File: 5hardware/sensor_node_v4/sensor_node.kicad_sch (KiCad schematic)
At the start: 19 parts, among them J4 Conn_02x20_Counter_Clockwise, J5 Conn_02x20_Counter_Clockwise, SW7 SW_DIP_x04, SW8 SW_Push, SW9 RotaryEncoder, U10 CH32V003F4P6, U11 MCP1700x-330xxTO, U12 APDS-9960, U14 DS3231M, U15 DS1307+, U16 DS1302+, U17 VL53L1CXV0FY1, U18 BH1750FVI-TR, Y1 Crystal

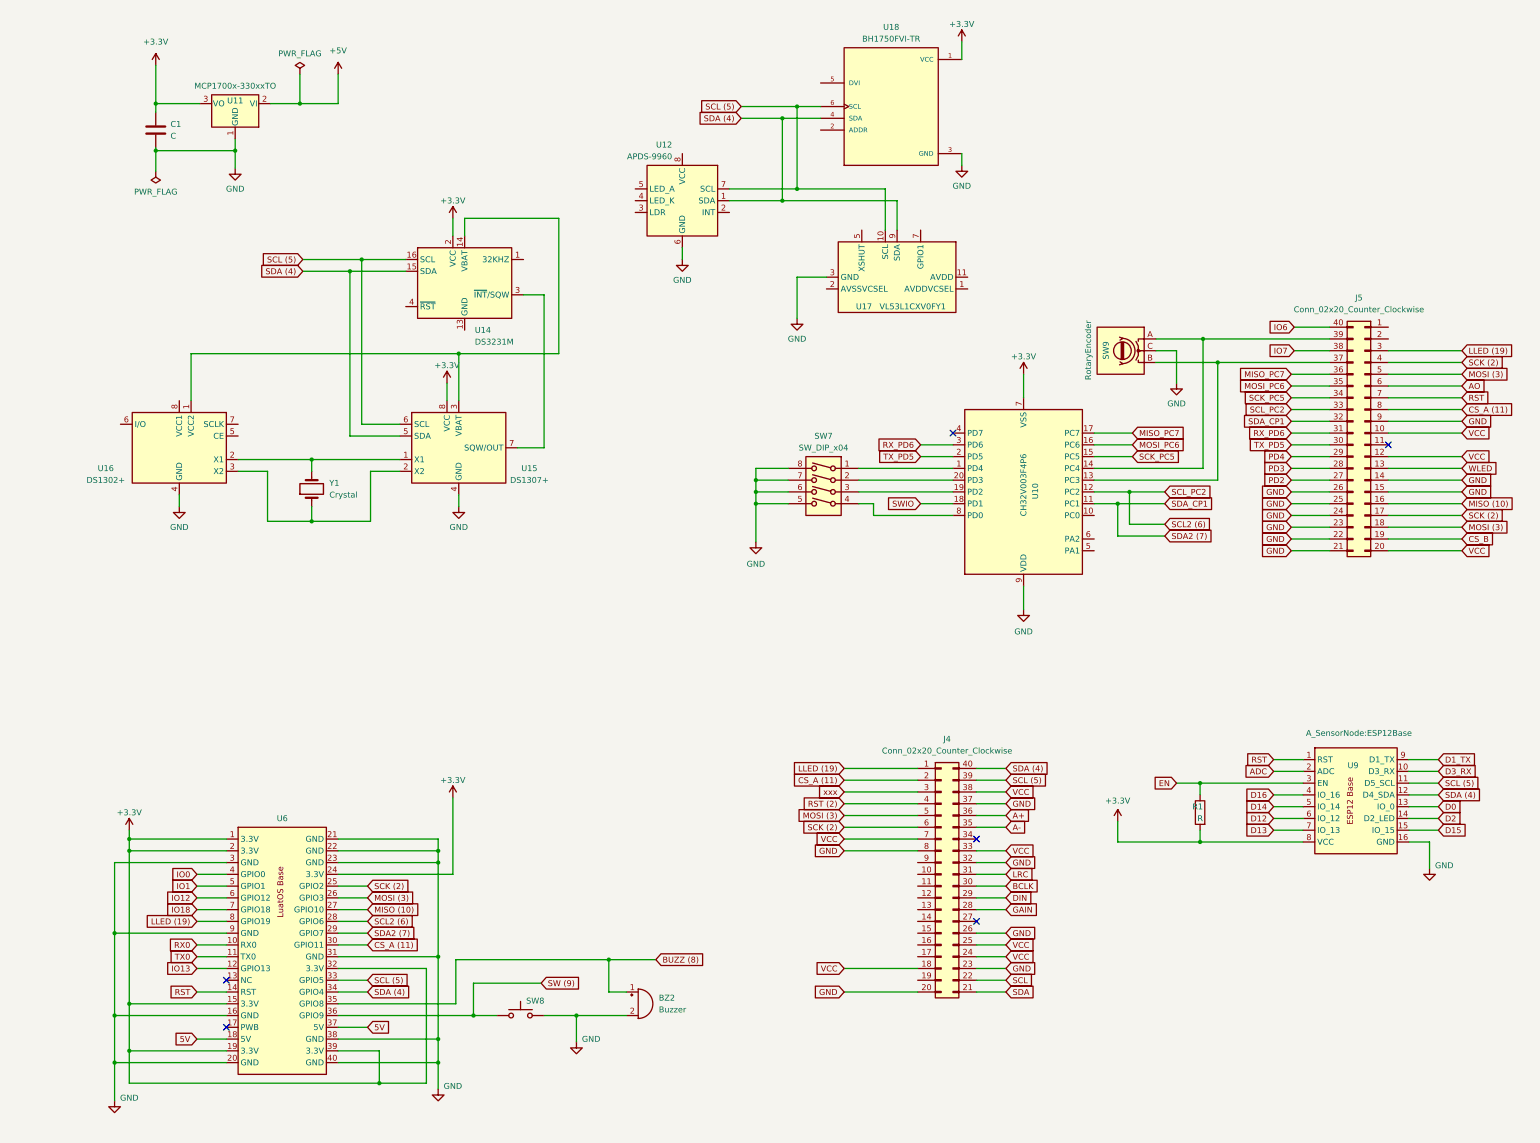
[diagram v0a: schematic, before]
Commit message: update SensorNode V4.0 schematic.
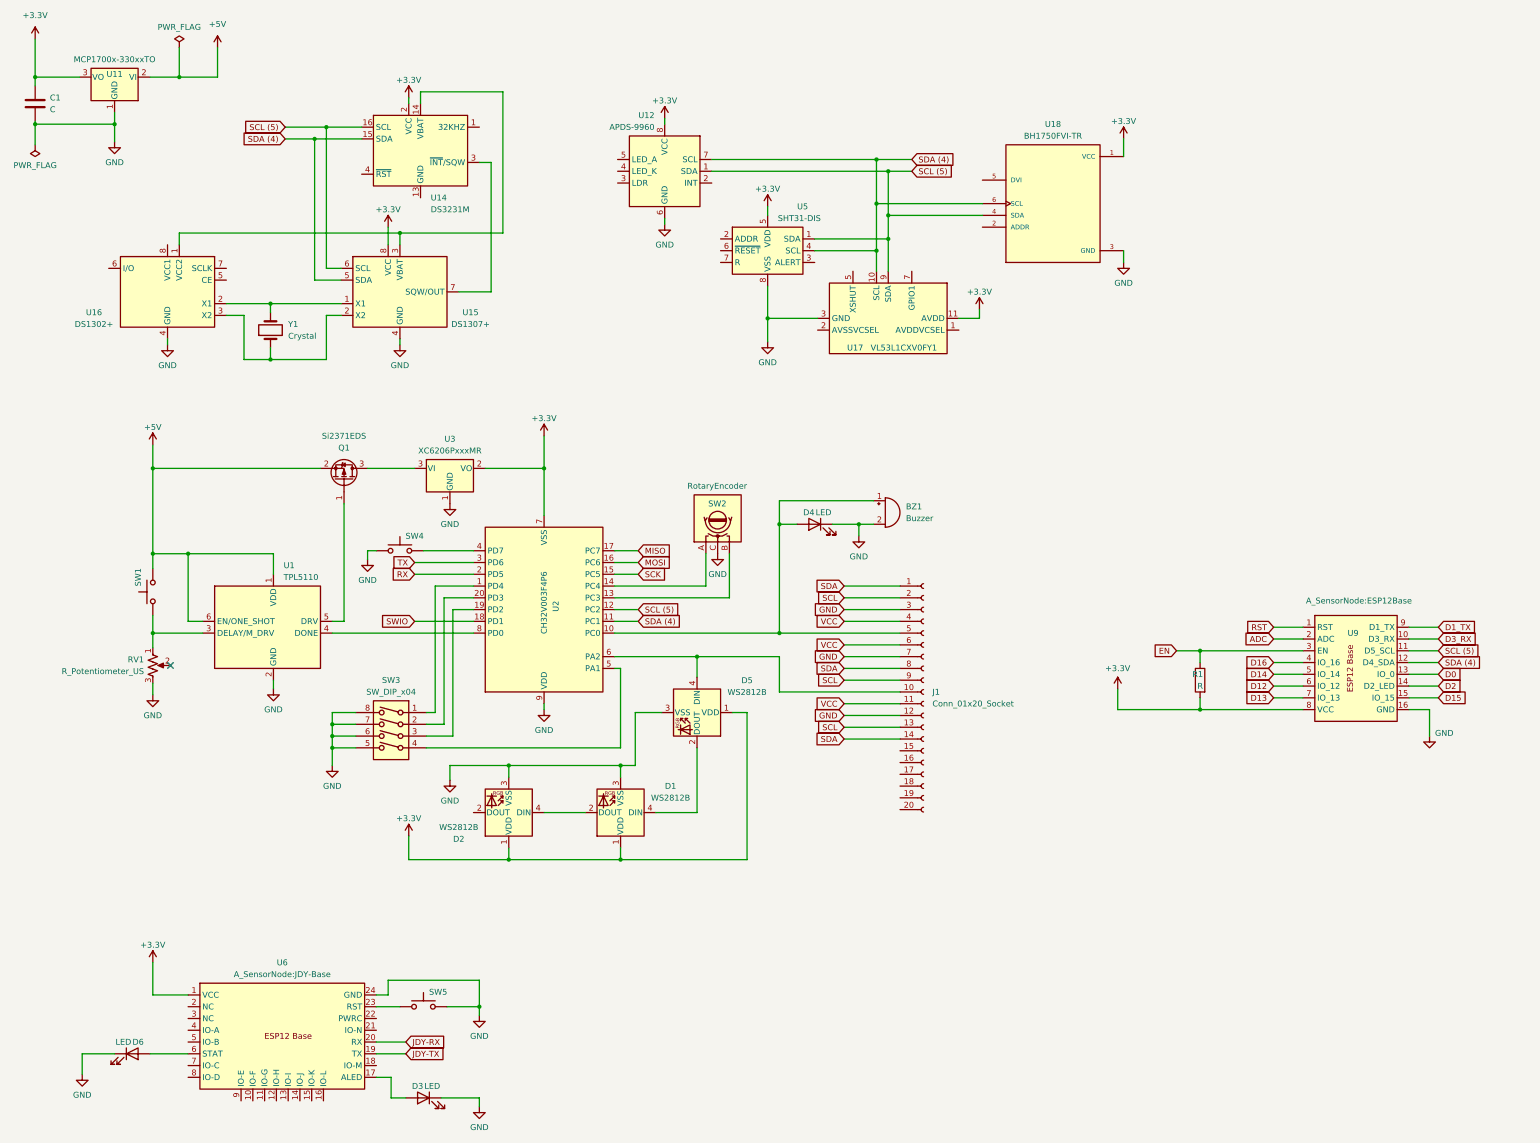
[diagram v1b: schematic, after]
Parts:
- removed BZ2: Buzzer, A_SensorNode:BuzzerSmall, symbol Device:Buzzer
- removed J4, J5: Conn_02x20_Counter_Clockwise, Connector_PinSocket_2.54mm:PinSocket_2x20_P2.54mm_Vertical, symbol Connector_Generic:Conn_02x20_Counter_Clockwise
- removed SW7: SW_DIP_x04, Button_Switch_SMD:SW_DIP_SPSTx04_Slide_6.7x11.72mm_W8.61mm_P2.54mm_LowProfile, symbol Switch:SW_DIP_x04
- removed SW8: SW_Push, Button_Switch_THT:SW_PUSH-12mm, symbol Switch:SW_Push
- removed SW9: RotaryEncoder, Rotary_Encoder:RotaryEncoder_Alps_EC11E_Vertical_H20mm, symbol Device:RotaryEncoder
- removed U10: CH32V003F4P6, Package_SO:TSSOP-20_4.4x6.5mm_P0.65mm, symbol wch-mcu:CH32V003F4P6
- removed U6: ~, symbol A_SensorNode:LuatOS_Base
- added BZ1: Buzzer, A_SensorNode:BuzzerSmall, symbol Device:Buzzer
- added D1, D2, D5: WS2812B, LED_SMD:LED_WS2812B_PLCC4_5.0x5.0mm_P3.2mm, symbol LED:WS2812B
- added D3, D4, D6: LED, symbol Device:LED
- added J1: Conn_01x20_Socket, symbol Connector:Conn_01x20_Socket
- added Q1: Si2371EDS, Package_TO_SOT_SMD:SOT-23, symbol Transistor_FET:Si2371EDS
- added RV1: R_Potentiometer_US, symbol Device:R_Potentiometer_US
- added SW1, SW4, SW5: SW_Push, Button_Switch_THT:SW_PUSH-12mm, symbol Switch:SW_Push
- added SW2: RotaryEncoder, Rotary_Encoder:RotaryEncoder_Alps_EC11E_Vertical_H20mm, symbol Device:RotaryEncoder
- added SW3: SW_DIP_x04, Button_Switch_SMD:SW_DIP_SPSTx04_Slide_6.7x11.72mm_W8.61mm_P2.54mm_LowProfile, symbol Switch:SW_DIP_x04
- added U1: TPL5110, Package_TO_SOT_SMD:SOT-23-6, symbol Timer:TPL5110
- added U2: CH32V003F4P6, Package_SO:TSSOP-20_4.4x6.5mm_P0.65mm, symbol wch-mcu:CH32V003F4P6
- added U3: XC6206PxxxMR, Package_TO_SOT_SMD:SOT-23-3, symbol Regulator_Linear:XC6206PxxxMR
- added U5: SHT31-DIS, Sensor_Humidity:Sensirion_DFN-8-1EP_2.5x2.5mm_P0.5mm_EP1.1x1.7mm, symbol Sensor_Humidity:SHT31-DIS
- added U6: ~, A_SensorNode:JDY-Base, symbol A_SensorNode:JDY-Base
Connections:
- net +3.3V: now also U12.8 (VCC), U17.11 (AVDD), D1.1 (VDD), D2.1 (VDD), D5.1 (VDD), U2.7 (VSS), U3.2 (VO), U5.5 (VDD), U6.1 (VCC)
- net +5V: now also Q1.2 (S), SW1.1, U1.1 (VDD), U1.6 (EN/ONE_SHOT)
- net GND: now also BZ1.2 (+), D1.3 (VSS), D2.3 (VSS), D3.1 (K), D4.1 (K), D5.3 (VSS), D6.1 (K), J1.12 (Pin_12), J1.3 (Pin_3), J1.7 (Pin_7), RV1.3, SW2.C, SW3.5, SW3.6, SW3.7, SW3.8, SW4.2, SW5.1, U1.2 (GND), U2.9 (VDD), U3.1 (GND), U5.8 (VSS), U5.9 (VSS), U6.24 (GND)
- net SCL: now also J1.13 (Pin_13), J1.2 (Pin_2), J1.9 (Pin_9)
- net SCL (5): now also U12.1 (SDA), U17.9 (SDA), U18.4 (SDA), U2.12 (PC2), U5.1 (SDA); no longer U12.7 (SCL), U17.10 (SCL), U18.6 (SCL)
- net SDA: now also J1.1 (Pin_1), J1.14 (Pin_14), J1.8 (Pin_8)
- net SDA (4): now also U12.7 (SCL), U17.10 (SCL), U18.6 (SCL), U2.11 (PC1), U5.4 (SCL); no longer U12.1 (SDA), U17.9 (SDA), U18.4 (SDA)
- net SWIO: now also U2.18 (PD1)
- net VCC: now also J1.11 (Pin_11), J1.4 (Pin_4), J1.6 (Pin_6)
- new net: SW2.A, U2.14 (PC4)
- new net: SW2.B, U2.13 (PC3)
- new net: D1.4 (DIN), D5.2 (DOUT)
- new net: D5.4 (DIN), J1.10 (Pin_10), U2.6 (PA2)
- new net: D6.2 (A), U6.6 (STAT)
- new net: BZ1.1 (-), D4.2 (A), J1.5 (Pin_5), U2.10 (PC0)
- new net: D1.2 (DOUT), D2.4 (DIN)
- new net: SW3.1, U2.1 (PD4)
- new net: SW3.2, U2.20 (PD3)
- new net: SW3.3, U2.19 (PD2)
- new net: SW3.4, U2.5 (PA1)
- new net: RV1.1, SW1.2, U1.3 (DELAY/M_DRV)
- new net: U1.4 (DONE), U2.8 (PD0)
- new net: Q1.1 (G), U1.5 (DRV)
- new net: D3.2 (A), U6.17 (ALED)
- new net: SW4.1, U2.4 (PD7)
- new net: SW5.2, U6.23 (RST)
- new net: Q1.3 (D), U3.3 (VI)
- new net JDY-RX: U6.20 (RX)
- new net JDY-TX: U6.19 (TX)
- new net MISO: U2.17 (PC7)
- new net MOSI: U2.16 (PC6)
- new net RX: U2.2 (PD5)
- new net SCK: U2.15 (PC5)
- new net TX: U2.3 (PD6)
- no-connect marks 6 -> 1
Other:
- moved on the sheet: C1, R1, U11, U12, U14, U15, U16, U17, U18, U9, Y1

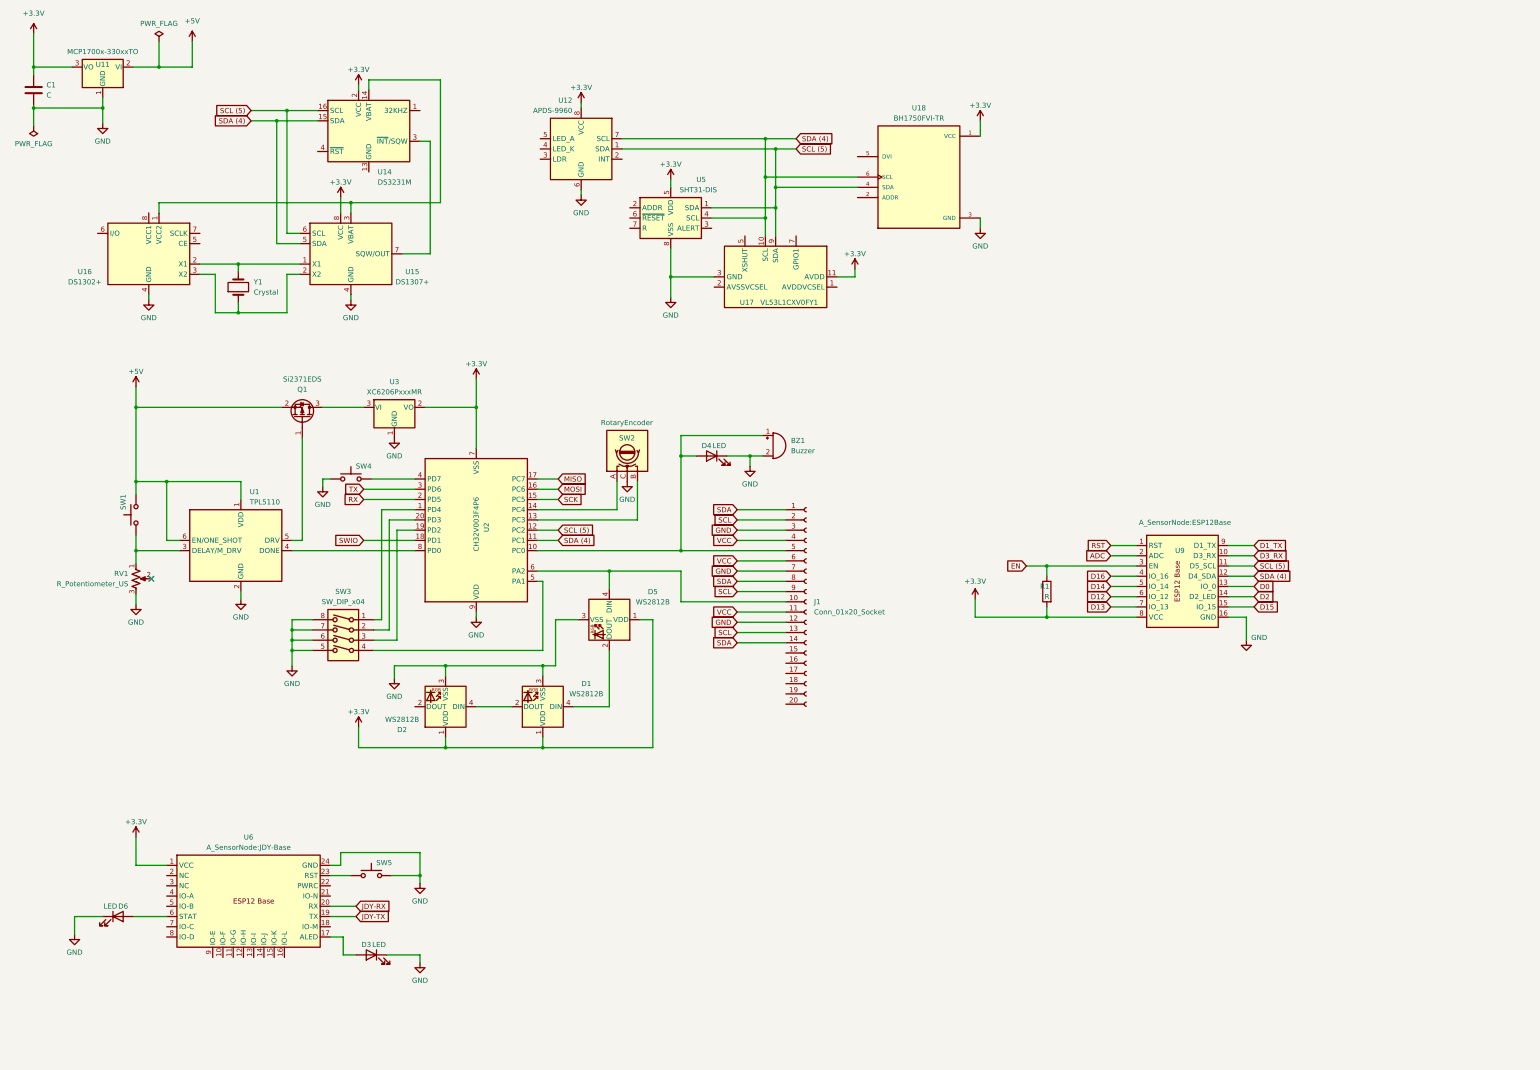
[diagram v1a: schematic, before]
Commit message: update schematic.
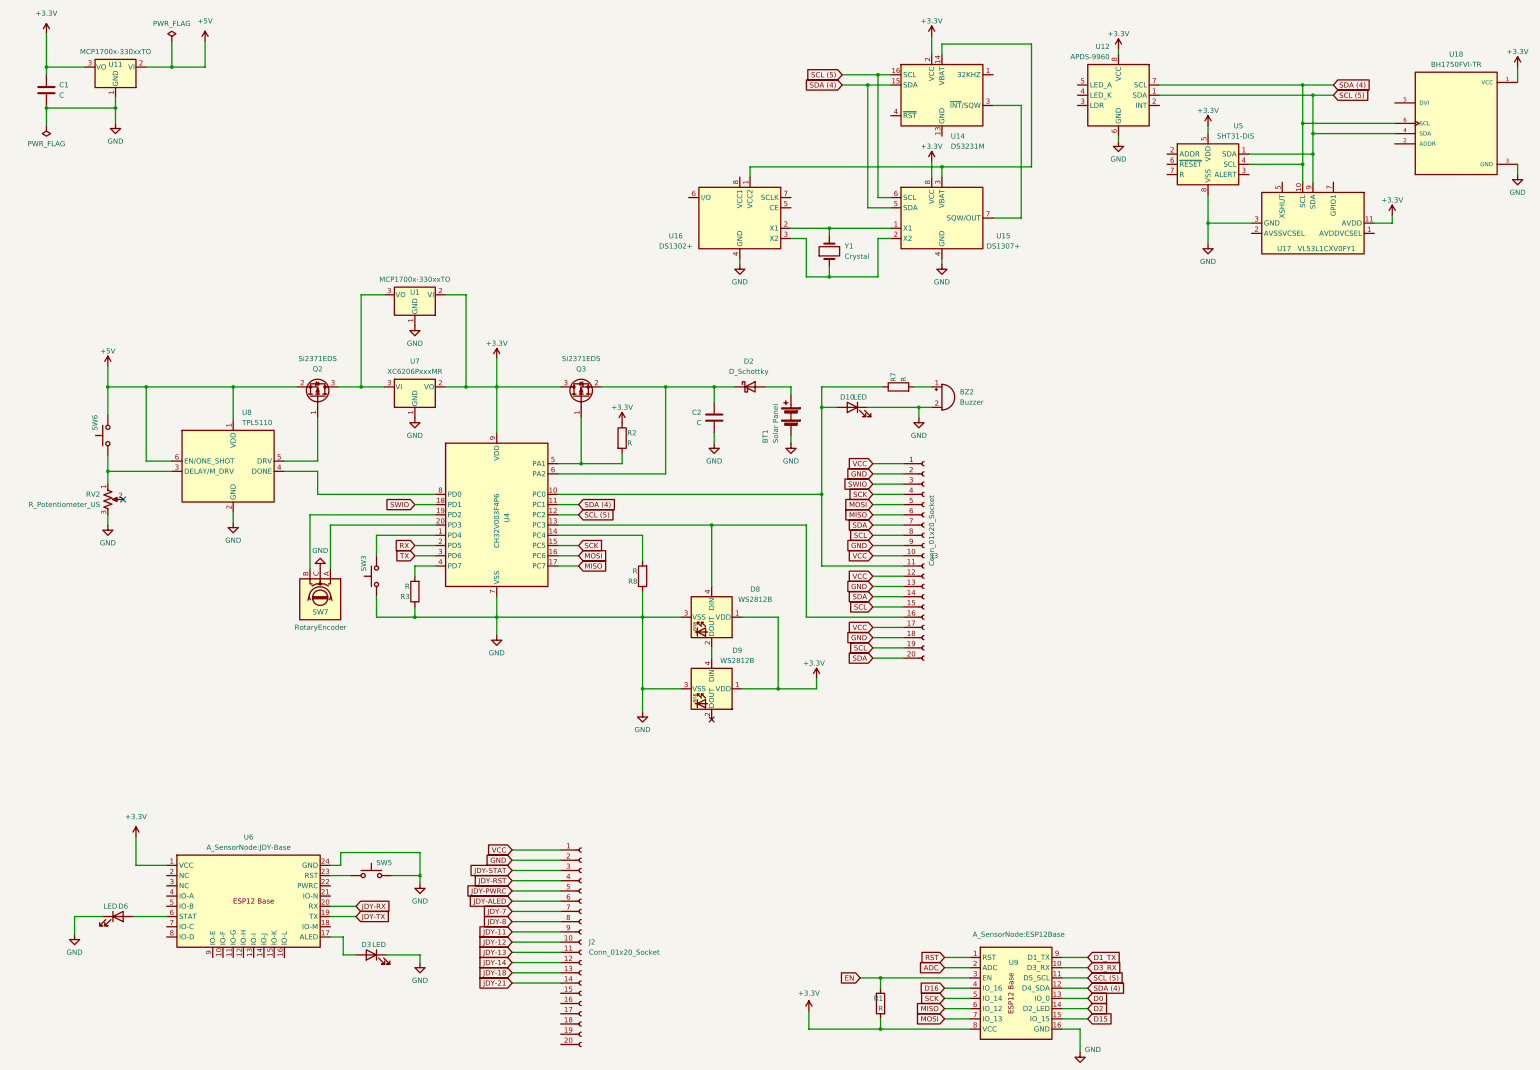
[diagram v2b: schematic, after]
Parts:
- removed BZ1: Buzzer, A_SensorNode:BuzzerSmall, symbol Device:Buzzer
- removed D1, D2, D5: WS2812B, LED_SMD:LED_WS2812B_PLCC4_5.0x5.0mm_P3.2mm, symbol LED:WS2812B
- removed D4: LED, symbol Device:LED
- removed J1: Conn_01x20_Socket, symbol Connector:Conn_01x20_Socket
- removed Q1: Si2371EDS, Package_TO_SOT_SMD:SOT-23, symbol Transistor_FET:Si2371EDS
- removed RV1: R_Potentiometer_US, symbol Device:R_Potentiometer_US
- removed SW1, SW4: SW_Push, Button_Switch_THT:SW_PUSH-12mm, symbol Switch:SW_Push
- removed SW2: RotaryEncoder, Rotary_Encoder:RotaryEncoder_Alps_EC11E_Vertical_H20mm, symbol Device:RotaryEncoder
- removed SW3: SW_DIP_x04, Button_Switch_SMD:SW_DIP_SPSTx04_Slide_6.7x11.72mm_W8.61mm_P2.54mm_LowProfile, symbol Switch:SW_DIP_x04
- removed U1: TPL5110, Package_TO_SOT_SMD:SOT-23-6, symbol Timer:TPL5110
- removed U2: CH32V003F4P6, Package_SO:TSSOP-20_4.4x6.5mm_P0.65mm, symbol wch-mcu:CH32V003F4P6
- removed U3: XC6206PxxxMR, Package_TO_SOT_SMD:SOT-23-3, symbol Regulator_Linear:XC6206PxxxMR
- added BT1: Solar Panel, symbol Device:Battery
- added BZ2: Buzzer, A_SensorNode:BuzzerSmall, symbol Device:Buzzer
- added C2: C, Capacitor_THT:CP_Radial_D5.0mm_P2.00mm, symbol Device:C
- added D10: LED, symbol Device:LED
- added D2: D_Schottky, symbol Device:D_Schottky
- added D8, D9: WS2812B, LED_SMD:LED_WS2812B_PLCC4_5.0x5.0mm_P3.2mm, symbol LED:WS2812B
- added J2, J3: Conn_01x20_Socket, symbol Connector:Conn_01x20_Socket
- added Q2, Q3: Si2371EDS, Package_TO_SOT_SMD:SOT-23, symbol Transistor_FET:Si2371EDS
- added R2, R3, R7, R8: R, symbol Device:R
- added RV2: R_Potentiometer_US, symbol Device:R_Potentiometer_US
- added SW3, SW6: SW_Push, Button_Switch_THT:SW_PUSH-12mm, symbol Switch:SW_Push
- added SW7: RotaryEncoder, Rotary_Encoder:RotaryEncoder_Alps_EC11E_Vertical_H20mm, symbol Device:RotaryEncoder
- added U1: MCP1700x-330xxTO, Package_TO_SOT_THT:TO-92_Inline, symbol Regulator_Linear:MCP1700x-330xxTO
- added U4: CH32V003F4P6, Package_SO:TSSOP-20_4.4x6.5mm_P0.65mm, symbol wch-mcu:CH32V003F4P6
- added U7: XC6206PxxxMR, Package_TO_SOT_SMD:SOT-23-3, symbol Regulator_Linear:XC6206PxxxMR
- added U8: TPL5110, Package_TO_SOT_SMD:SOT-23-6, symbol Timer:TPL5110
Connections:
- net D12 is gone; now on net MISO: U9.6 (IO_12)
- net D13 is gone; now on net MOSI: U9.7 (IO_13)
- net D14 is gone; now on net SCK: U9.5 (IO_14)
- net +3.3V: now also D8.1 (VDD), D9.1 (VDD), Q3.3 (D), R2.1, U1.2 (VI), U4.9 (VDD), U7.2 (VO)
- net +5V: now also Q2.2 (S), SW6.1, U8.1 (VDD), U8.6 (EN/ONE_SHOT)
- net GND: now also BT1.2 (-), BZ2.2 (+), C2.2, D10.1 (K), D8.3 (VSS), D9.3 (VSS), J2.2 (Pin_2), J3.13 (Pin_13), J3.18 (Pin_18), J3.2 (Pin_2), J3.9 (Pin_9), R3.1, R8.1, RV2.3, SW3.2, SW7.C, U1.1 (GND), U4.7 (VSS), U7.1 (GND), U8.2 (GND)
- net MISO: now also J3.6 (Pin_6), U4.17 (PC7)
- net MOSI: now also J3.5 (Pin_5), U4.16 (PC6)
- net RX: now also U4.2 (PD5)
- net SCK: now also J3.4 (Pin_4), U4.15 (PC5)
- net SCL: now also J3.15 (Pin_15), J3.19 (Pin_19), J3.8 (Pin_8)
- net SCL (5): now also U4.12 (PC2)
- net SDA: now also J3.14 (Pin_14), J3.20 (Pin_20), J3.7 (Pin_7)
- net SDA (4): now also U4.11 (PC1)
- net SWIO: now also J3.3 (Pin_3), U4.18 (PD1)
- net TX: now also U4.3 (PD6)
- net VCC: now also J2.1 (Pin_1), J3.1 (Pin_1), J3.10 (Pin_10), J3.12 (Pin_12), J3.17 (Pin_17)
- new net: RV2.1, SW6.2, U8.3 (DELAY/M_DRV)
- new net: Q2.1 (G), U8.5 (DRV)
- new net: Q2.3 (D), U1.3 (VO), U7.3 (VI)
- new net: U4.8 (PD0), U8.4 (DONE)
- new net: BZ2.1 (-), R7.2
- new net: SW3.1, U4.1 (PD4)
- new net: Q3.1 (G), R2.2, U4.5 (PA1)
- new net: C2.1, D2.1 (K), Q3.2 (S), U4.6 (PA2)
- new net: D10.2 (A), J3.11 (Pin_11), R7.1, U4.10 (PC0)
- new net: D8.4 (DIN), J3.16 (Pin_16), U4.13 (PC3)
- new net: R8.2, U4.14 (PC4)
- new net: SW7.B, U4.19 (PD2)
- new net: SW7.A, U4.20 (PD3)
- new net: R3.2, U4.4 (PD7)
- new net: D8.2 (DOUT), D9.4 (DIN)
- new net: BT1.1 (+), D2.2 (A)
- new net JDY-11: J2.9 (Pin_9)
- new net JDY-12: J2.10 (Pin_10)
- new net JDY-13: J2.11 (Pin_11)
- new net JDY-14: J2.12 (Pin_12)
- new net JDY-18: J2.13 (Pin_13)
- new net JDY-21: J2.14 (Pin_14)
- new net JDY-7: J2.7 (Pin_7)
- new net JDY-8: J2.8 (Pin_8)
- new net JDY-ALED: J2.6 (Pin_6)
- new net JDY-PWRC: J2.5 (Pin_5)
- new net JDY-RST: J2.4 (Pin_4)
- new net JDY-STAT: J2.3 (Pin_3)
- no-connect marks 1 -> 2
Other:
- moved on the sheet: C1, R1, U11, U12, U14, U15, U16, U17, U18, U5, U9, Y1
